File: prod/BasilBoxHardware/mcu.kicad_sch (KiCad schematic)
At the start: 6 parts, among them U1 NUCLEO64-F411RE, U2 ST-Link

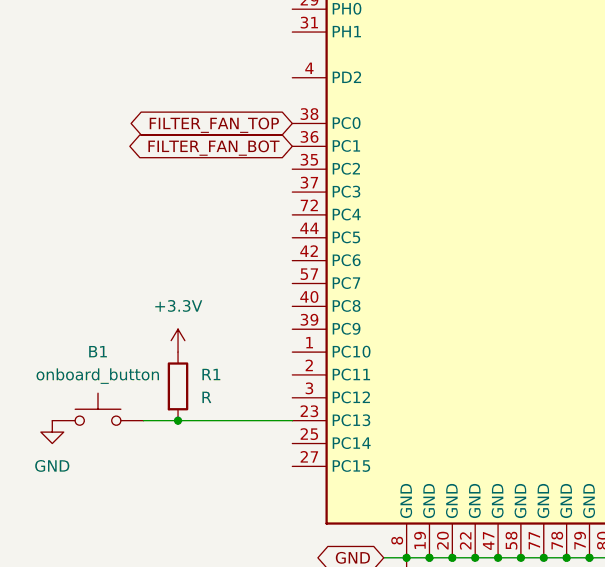
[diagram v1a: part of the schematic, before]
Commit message: Add led light control
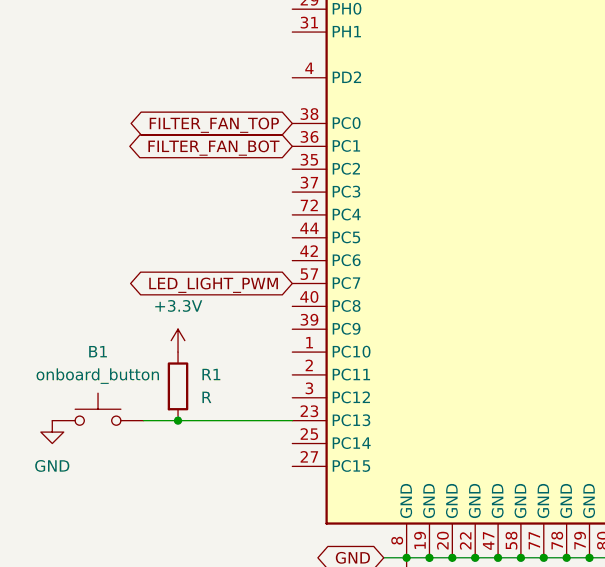
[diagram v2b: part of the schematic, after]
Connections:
- net LED_LIGHT_PWM: now reaches U1.57 (PC7)
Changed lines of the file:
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@@
+    )
+  )
+  (global_label "LED_LIGHT_PWM" (shape bidirectional) (at 114.3 115.57 180) (fields_autoplaced)
+    (effects (font (size 1.27 1.27)) (justify right))
+    (property "Intersheet References" "${INTERSHEET_REFS}" (id 0) (at 97.1307 115.4906 0)
+      (effects (font (size 1.27 1.27)) (justify right) hide)
     )
   )

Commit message: Add hardware schematics
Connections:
- net SDIO_D2: now reaches U1.1 (PC10)
- net SDIO_D3: now reaches U1.2 (PC11)
- net SDIO_D0: now reaches U1.21 (PB7)
- net SDIO_CK: now reaches U1.3 (PC12)
- net SDIO_DETECT: now reaches U1.35 (PC2)
- net SDIO_D1: now reaches U1.39 (PC9)
- net SDIO_CMD: now reaches U1.4 (PD2)
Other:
- moved on the sheet: B1, R1
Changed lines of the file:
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@@
   (junction (at 132.08 146.05) (diameter 0) (color 0 0 0 0)
   )
-  (junction (at 101.6 130.81) (diameter 0) (color 0 0 0 0)
-  )
   (junction (at 142.24 146.05) (diameter 0) (color 0 0 0 0)
   )
@@
   (junction (at 127 41.91) (diameter 0) (color 0 0 0 0)
   )
+  (junction (at 93.98 130.81) (diameter 0) (color 0 0 0 0)
+  )
   (junction (at 144.78 146.05) (diameter 0) (color 0 0 0 0)
   )
@@
     (stroke (width 0) (type default) (color 0 0 0 0))
   )
-  (wire (pts (xy 97.79 130.81) (xy 101.6 130.81))
+  (wire (pts (xy 91.44 130.81) (xy 93.98 130.81))
     (stroke (width 0) (type default) (color 0 0 0 0))
   )
@@
     (stroke (width 0) (type default) (color 0 0 0 0))
   )
+  (wire (pts (xy 81.28 133.35) (xy 81.28 130.81))
+    (stroke (width 0) (type default) (color 0 0 0 0))
+  )
   (wire (pts (xy 127 41.91) (xy 132.08 41.91))
     (stroke (width 0) (type default) (color 0 0 0 0))
@@
     (stroke (width 0) (type default) (color 0 0 0 0))
   )
-  (wire (pts (xy 101.6 130.81) (xy 114.3 130.81))
+  (wire (pts (xy 93.98 130.81) (xy 114.3 130.81))
     (stroke (width 0) (type default) (color 0 0 0 0))
   )
@@
     )
   )
+  (global_label "SDIO_CMD" (shape bidirectional) (at 114.3 92.71 180) (fields_autoplaced)
+    (effects (font (size 1.27 1.27)) (justify right))
+    (property "Intersheet References" "${INTERSHEET_REFS}" (id 0) (at 102.5131 92.6306 0)
+      (effects (font (size 1.27 1.27)) (justify right) hide)
+    )
+  )
+  (global_label "SDIO_D2" (shape bidirectional) (at 114.3 123.19 180) (fields_autoplaced)
+    (effects (font (size 1.27 1.27)) (justify right))
+    (property "Intersheet References" "${INTERSHEET_REFS}" (id 0) (at 104.025 123.1106 0)
+      (effects (font (size 1.27 1.27)) (justify right) hide)
+    )
+  )
   (global_label "GND" (shape bidirectional) (at 124.46 146.05 180) (fields_autoplaced)
     (effects (font (size 1.27 1.27)) (justify right))
@@
     )
   )
+  (global_label "SDIO_D1" (shape bidirectional) (at 114.3 120.65 180) (fields_autoplaced)
+    (effects (font (size 1.27 1.27)) (justify right))
+    (property "Intersheet References" "${INTERSHEET_REFS}" (id 0) (at 104.025 120.5706 0)
+      (effects (font (size 1.27 1.27)) (justify right) hide)
+    )
+  )
+  (global_label "SDIO_CK" (shape bidirectional) (at 114.3 128.27 180) (fields_autoplaced)
+    (effects (font (size 1.27 1.27)) (justify right))
+    (property "Intersheet References" "${INTERSHEET_REFS}" (id 0) (at 103.9645 128.1906 0)
+      (effects (font (size 1.27 1.27)) (justify right) hide)
+    )
+  )
+  (global_label "SDIO_D0" (shape bidirectional) (at 170.18 118.11 0) (fields_autoplaced)
+    (effects (font (size 1.27 1.27)) (justify left))
+    (property "Intersheet References" "${INTERSHEET_REFS}" (id 0) (at 180.455 118.0306 0)
+      (effects (font (size 1.27 1.27)) (justify left) hide)
+    )
+  )
+  (global_label "SDIO_DETECT" (shape bidirectional) (at 114.3 102.87 180) (fields_autoplaced)
+    (effects (font (size 1.27 1.27)) (justify right))
+    (property "Intersheet References" "${INTERSHEET_REFS}" (id 0) (at 99.7312 102.7906 0)
+      (effects (font (size 1.27 1.27)) (justify right) hide)
+    )
+  )
   (global_label "FILTER_FAN_BOT" (shape bidirectional) (at 114.3 100.33 180) (fields_autoplaced)
     (effects (font (size 1.27 1.27)) (justify right))
     (property "Intersheet References" "${INTERSHEET_REFS}" (id 0) (at 96.7679 100.2506 0)
+      (effects (font (size 1.27 1.27)) (justify right) hide)
+    )
+  )
+  (global_label "SDIO_D3" (shape bidirectional) (at 114.3 125.73 180) (fields_autoplaced)
+    (effects (font (size 1.27 1.27)) (justify right))
+    (property "Intersheet References" "${INTERSHEET_REFS}" (id 0) (at 104.025 125.6506 0)
       (effects (font (size 1.27 1.27)) (justify right) hide)
     )
@@
     (pin "1")
   )
-  (symbol (lib_id "power:GND") (at 87.63 130.81 0) (unit 1)
-    (in_bom yes) (on_board yes) (fields_autoplaced)
-    (property "Reference" "#PWR?" (id 0) (at 87.63 137.16 0)
-      (effects (font (size 1.27 1.27)) hide)
-    )
-    (property "Value" "GND" (id 1) (at 87.63 135.89 0))
-    (property "Footprint" "" (id 2) (at 87.63 130.81 0)
-      (effects (font (size 1.27 1.27)) hide)
-    )
-    (property "Datasheet" "" (id 3) (at 87.63 130.81 0)
-      (effects (font (size 1.27 1.27)) hide)
-    )
-    (pin "1")
-  )
-  (symbol (lib_id "Switch:SW_Push") (at 92.71 130.81 0) (unit 1)
-    (in_bom yes) (on_board yes) (fields_autoplaced)
-    (property "Reference" "B1" (id 0) (at 92.71 123.19 0))
-    (property "Value" "onboard_button" (id 1) (at 92.71 125.73 0))
-    (property "Footprint" "" (id 2) (at 92.71 125.73 0)
-      (effects (font (size 1.27 1.27)) hide)
-    )
-    (property "Datasheet" "~" (id 3) (at 92.71 125.73 0)
+  (symbol (lib_id "power:GND") (at 81.28 133.35 0) (unit 1)
+    (in_bom yes) (on_board yes) (fields_autoplaced)
+    (property "Reference" "#PWR?" (id 0) (at 81.28 139.7 0)
+      (effects (font (size 1.27 1.27)) hide)
+    )
+    (property "Value" "GND" (id 1) (at 81.28 138.43 0))
+    (property "Footprint" "" (id 2) (at 81.28 133.35 0)
+      (effects (font (size 1.27 1.27)) hide)
+    )
+    (property "Datasheet" "" (id 3) (at 81.28 133.35 0)
+      (effects (font (size 1.27 1.27)) hide)
+    )
+    (pin "1")
+  )
+  (symbol (lib_id "Switch:SW_Push") (at 86.36 130.81 0) (unit 1)
+    (in_bom yes) (on_board yes) (fields_autoplaced)
+    (property "Reference" "B1" (id 0) (at 86.36 123.19 0))
+    (property "Value" "onboard_button" (id 1) (at 86.36 125.73 0))
+    (property "Footprint" "" (id 2) (at 86.36 125.73 0)
+      (effects (font (size 1.27 1.27)) hide)
+    )
+    (property "Datasheet" "~" (id 3) (at 86.36 125.73 0)
       (effects (font (size 1.27 1.27)) hide)
     )
@@
     (pin "1")
   )
-  (symbol (lib_id "Device:R") (at 101.6 127 0) (unit 1)
-    (in_bom yes) (on_board yes) (fields_autoplaced)
-    (property "Reference" "R1" (id 0) (at 104.14 125.7299 0)
+  (symbol (lib_id "Device:R") (at 93.98 127 0) (unit 1)
+    (in_bom yes) (on_board yes) (fields_autoplaced)
+    (property "Reference" "R1" (id 0) (at 96.52 125.7299 0)
       (effects (font (size 1.27 1.27)) (justify left))
     )
-    (property "Value" "R" (id 1) (at 104.14 128.2699 0)
+    (property "Value" "R" (id 1) (at 96.52 128.2699 0)
       (effects (font (size 1.27 1.27)) (justify left))
     )
-    (property "Footprint" "" (id 2) (at 99.822 127 90)
-      (effects (font (size 1.27 1.27)) hide)
-    )
-    (property "Datasheet" "~" (id 3) (at 101.6 127 0)
+    (property "Footprint" "" (id 2) (at 92.202 127 90)
+      (effects (font (size 1.27 1.27)) hide)
+    )
+    (property "Datasheet" "~" (id 3) (at 93.98 127 0)
       (effects (font (size 1.27 1.27)) hide)
     )
@@
     (pin "2")
   )
-  (symbol (lib_id "power:+3.3V") (at 101.6 123.19 0) (unit 1)
-    (in_bom yes) (on_board yes) (fields_autoplaced)
-    (property "Reference" "#PWR?" (id 0) (at 101.6 127 0)
-      (effects (font (size 1.27 1.27)) hide)
-    )
-    (property "Value" "+3.3V" (id 1) (at 101.6 118.11 0))
-    (property "Footprint" "" (id 2) (at 101.6 123.19 0)
-      (effects (font (size 1.27 1.27)) hide)
-    )
-    (property "Datasheet" "" (id 3) (at 101.6 123.19 0)
-      (effects (font (size 1.27 1.27)) hide)
-    )
+  (symbol (lib_id "power:+3.3V") (at 93.98 123.19 0) (unit 1)
+    (in_bom yes) (on_board yes) (fields_autoplaced)
+    (property "Reference" "#PWR?" (id 0) (at 93.98 127 0)
+      (effects (font (size 1.27 1.27)) hide)
+    )
+    (property "Value" "+3.3V" (id 1) (at 93.98 118.11 0))
+    (property "Footprint" "" (id 2) (at 93.98 123.19 0)
+      (effects (font (size 1.27 1.27)) hide)
+    )
+    (property "Datasheet" "" (id 3) (at 93.98 123.19 0)
+      (effects (font (size 1.27 1.27)) hide)
+    )
